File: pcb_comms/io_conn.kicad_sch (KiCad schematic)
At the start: 15 parts, among them IC1 CP2102N-A02-GQFN28, J1 Conn_01x06_Pin, J2 USB_B_Micro

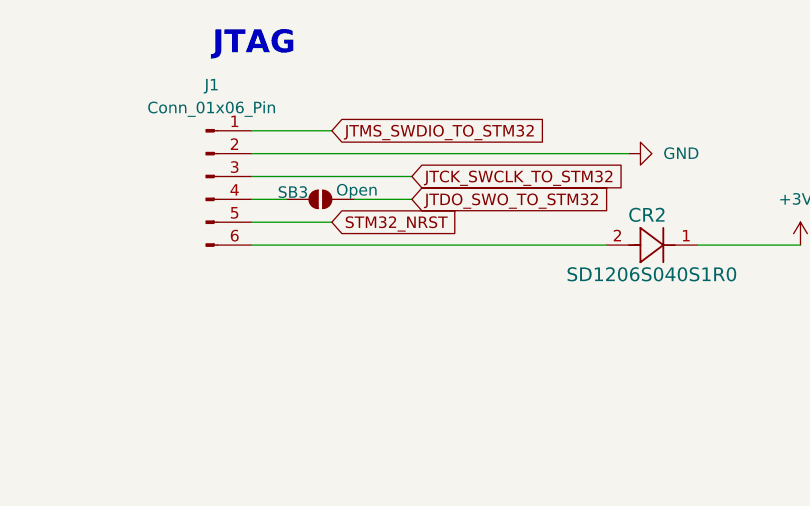
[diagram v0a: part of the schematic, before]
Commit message: Add external circuit for gps
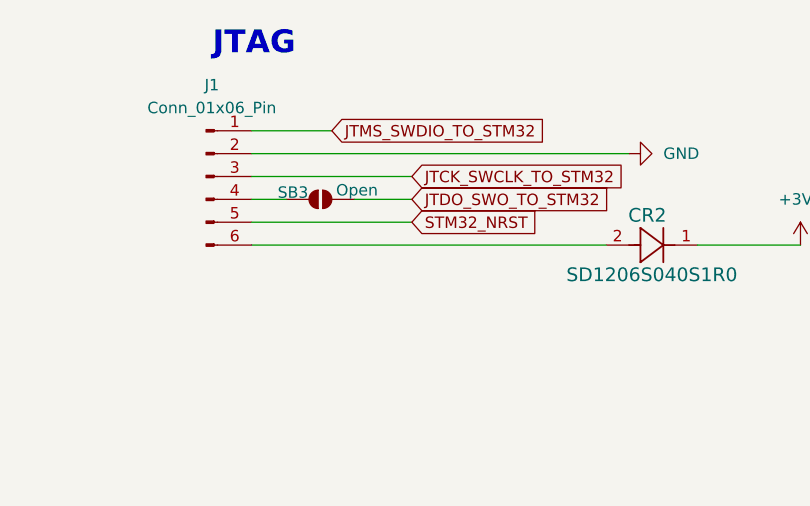
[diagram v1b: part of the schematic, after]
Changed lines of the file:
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@@
 	(wire
 		(pts
-			(xy 208.28 39.37) (xy 217.17 39.37)
+			(xy 208.28 39.37) (xy 226.06 39.37)
 		)
 		(stroke
@@
 	(global_label "STM32_NRST"
 		(shape input)
-		(at 217.17 39.37 0)
+		(at 226.06 39.37 0)
 		(fields_autoplaced yes)
 		(effects
@@
 		)
 		(property "Intersheetrefs" "${INTERSHEET_REFS}"
-			(at 231.9479 39.37 0)
+			(at 240.8379 39.37 0)
 			(effects
 				(font

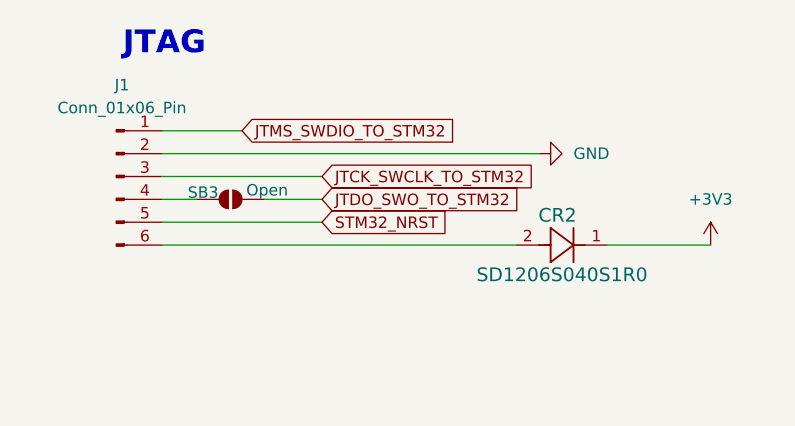
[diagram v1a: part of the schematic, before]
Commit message: Update GPS to pasive antenna
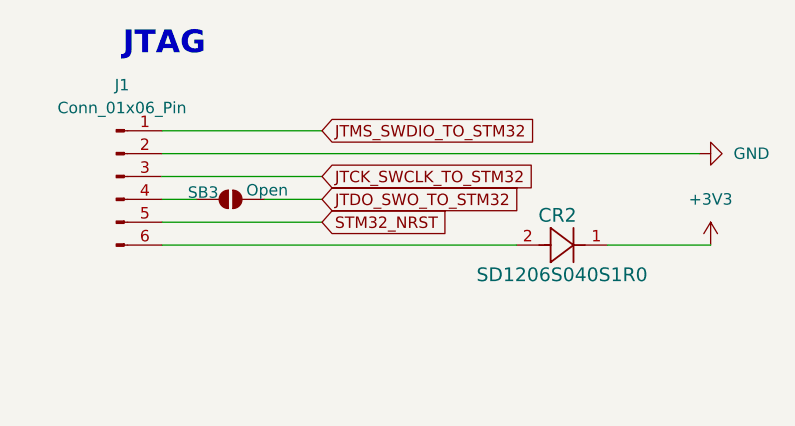
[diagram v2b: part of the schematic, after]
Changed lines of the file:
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@@
 	(wire
 		(pts
-			(xy 208.28 29.21) (xy 217.17 29.21)
+			(xy 208.28 29.21) (xy 226.06 29.21)
 		)
 		(stroke
@@
 	(wire
 		(pts
-			(xy 208.28 31.75) (xy 250.19 31.75)
+			(xy 208.28 31.75) (xy 267.97 31.75)
 		)
 		(stroke
@@
 	(global_label "JTMS_SWDIO_TO_STM32"
 		(shape input)
-		(at 217.17 29.21 0)
+		(at 226.06 29.21 0)
 		(fields_autoplaced yes)
 		(effects
@@
 		)
 		(property "Intersheetrefs" "${INTERSHEET_REFS}"
-			(at 241.8659 29.21 0)
+			(at 250.7559 29.21 0)
 			(effects
 				(font
@@
 	(symbol
 		(lib_id "power:GND")
-		(at 250.19 31.75 90)
+		(at 267.97 31.75 90)
 		(unit 1)
 		(exclude_from_sim no)
@@
 		(fields_autoplaced yes)
 		(property "Reference" "#PWR042"
-			(at 256.54 31.75 0)
+			(at 274.32 31.75 0)
 			(effects
 				(font
@@
 		)
 		(property "Value" "GND"
-			(at 254 31.7499 90)
+			(at 271.78 31.7499 90)
 			(effects
 				(font
@@
 		)
 		(property "Footprint" ""
-			(at 250.19 31.75 0)
+			(at 267.97 31.75 0)
 			(effects
 				(font
@@
 		)
 		(property "Datasheet" ""
-			(at 250.19 31.75 0)
+			(at 267.97 31.75 0)
 			(effects
 				(font
@@
 		)
 		(property "Description" "Power symbol creates a global label with name \"GND\" , ground"
-			(at 250.19 31.75 0)
-			(effects
-				(font
+			(at 267.97 31.75 0)
+			(effects
+				(font

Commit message: Update GPS
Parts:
- added J3, J5: OBC_I2C, symbol Connector_Generic:Conn_01x02
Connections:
- net GND: now also J5.2 (Pin_2)
- new net I2C1_SCL: J3.1 (Pin_1)
- new net I2C1_SDA: J3.2 (Pin_2)
- new net VBAT: J5.1 (Pin_1)
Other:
- note added: "FROM EPS"
- note added: "TO OBC"

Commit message: Add antenna deploy
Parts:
- added C47: 100uF, symbol Device:C
- added C48: 10uF, symbol Device:C
- added D6: Green, symbol Device:LED
- added J6: OBC_I2C, symbol Connector_Generic:Conn_01x02
- added R9: 1k, Resistor_SMD:R_0805_2012Metric, symbol Device:R
- added U6: ADP122AUJZ-3.3-R7, ADP122AUJZ_3_3_R7:UJ_5_ADI, symbol LDO_ADP122AUJZ_3_3_R7:ADP122AUJZ-3.3-R7
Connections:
- net GND: now also C47.2, C48.2, J6.2 (Pin_2), R9.1, U6.2 (GND)
- net USB_5V: now also C47.1, U6.1 (VIN), U6.3 (EN)
- net +3.3V renamed +3.3V_USB
- net +3.3V_USB: now also C48.1, D6.2 (A), U6.5 (VOUT)
- new net: D6.1 (K), R9.2
- new net BATT_FULL: J6.1 (Pin_1)
- no-connect marks 18 -> 19
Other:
- note added: "LDO 5V TO 3V3 (USB)"

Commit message: Update USB
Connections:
- net VBUS: now reaches CR1.2, D2.2 (K), J2.1 (VBUS)
- net VBUS: now also R2.1
- net +3.3V_USB renamed +3.3V
- net USB_5V renamed +5V
- net +5V: no longer R2.1

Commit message: Last update
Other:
- company: (none) -> Sanie Peralta, Alejandro Campo
- title: (none) -> PC1: APRS & GPS
- moved on the sheet: C48, D6, R9
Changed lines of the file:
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@@
 	(generator_version "9.0")
 	(paper "A4")
+	(title_block
+		(title "PC1: APRS & GPS")
+		(date "2026-04-01")
+		(rev "1.0")
+		(company "Sanie Peralta, Alejandro Campo")
+		(comment 1 "Introducción a la Ingeniería Satelital ")
+		(comment 2 "Primer Parcial")
+	)
 	(text "TO OBC"
 		(exclude_from_sim no)
@@
 	)
 	(junction
-		(at 135.89 161.29)
+		(at 124.46 161.29)
 		(diameter 0)
 		(color 0 0 0 0)
@@
 	)
 	(junction
-		(at 120.65 161.29)
+		(at 109.22 161.29)
 		(diameter 0)
 		(color 0 0 0 0)
@@
 	(wire
 		(pts
-			(xy 135.89 161.29) (xy 148.59 161.29)
+			(xy 124.46 161.29) (xy 137.16 161.29)
 		)
 		(stroke
@@
 	(wire
 		(pts
-			(xy 120.65 161.29) (xy 135.89 161.29)
+			(xy 109.22 161.29) (xy 124.46 161.29)
 		)
 		(stroke
@@
 	(wire
 		(pts
-			(xy 120.65 170.18) (xy 120.65 177.8)
+			(xy 109.22 170.18) (xy 109.22 177.8)
 		)
 		(stroke
@@
 	(wire
 		(pts
-			(xy 135.89 163.83) (xy 135.89 161.29)
+			(xy 124.46 163.83) (xy 124.46 161.29)
 		)
 		(stroke
@@
 	(wire
 		(pts
-			(xy 120.65 162.56) (xy 120.65 161.29)
+			(xy 109.22 162.56) (xy 109.22 161.29)
 		)
 		(stroke
@@
 	(wire
 		(pts
-			(xy 102.87 161.29) (xy 120.65 161.29)
+			(xy 102.87 161.29) (xy 109.22 161.29)
 		)
 		(stroke
@@
 	(wire
 		(pts
-			(xy 135.89 171.45) (xy 135.89 173.99)
+			(xy 124.46 171.45) (xy 124.46 173.99)
 		)
 		(stroke
@@
 	(wire
 		(pts
-			(xy 120.65 185.42) (xy 120.65 187.96)
+			(xy 109.22 185.42) (xy 109.22 187.96)
 		)
 		(stroke
@@
 	(symbol
 		(lib_id "Device:R")
-		(at 120.65 181.61 180)
+		(at 109.22 181.61 180)
 		(unit 1)
 		(exclude_from_sim no)
@@
 		(fields_autoplaced yes)
 		(property "Reference" "R9"
-			(at 123.19 180.3399 0)
+			(at 111.76 180.3399 0)
 			(effects
 				(font
@@
 		)
 		(property "Value" "1k"
-			(at 123.19 182.8799 0)
+			(at 111.76 182.8799 0)
 			(effects
 				(font
@@
 		)
 		(property "Footprint" "Resistor_SMD:R_0805_2012Metric"
-			(at 122.428 181.61 90)
+			(at 110.998 181.61 90)
 			(effects
 				(font
@@
 		)
 		(property "Datasheet" "~"
-			(at 120.65 181.61 0)
+			(at 109.22 181.61 0)
 			(effects
 				(font
@@
 		)
 		(property "Description" "Resistor"
-			(at 120.65 181.61 0)
+			(at 109.22 181.61 0)
 			(effects
 				(font
@@
 		)
 		(property "AVAILABILITY" ""
-			(at 120.65 181.61 0)
+			(at 109.22 181.61 0)
 			(effects
 				(font
@@
 		)
 		(property "DESCRIPTION" ""
-			(at 120.65 181.61 0)
+			(at 109.22 181.61 0)
 			(effects
 				(font
@@
 		)
 		(property "PACKAGE" ""
-			(at 120.65 181.61 0)
+			(at 109.22 181.61 0)
 			(effects
 				(font
@@
 		)
 		(property "PART_REV" ""
-			(at 120.65 181.61 0)
+			(at 109.22 181.61 0)
 			(effects
 				(font
@@
 		)
 		(property "PRICE" ""
-			(at 120.65 181.61 0)
+			(at 109.22 181.61 0)
 			(effects
 				(font
@@
 	(symbol
 		(lib_id "power:+3.3V")
-		(at 148.59 161.29 270)
+		(at 137.16 161.29 270)
 		(unit 1)
 		(exclude_from_sim no)
@@
 		(dnp no)
 		(property "Reference" "#PWR044"
-			(at 144.78 161.29 0)
+			(at 133.35 161.29 0)
 			(effects
 				(font
@@
 		)
 		(property "Value" "+3.3V"
-			(at 154.686 161.036 90)
+			(at 143.256 161.036 90)
 			(effects
 				(font
@@
 		)
 		(property "Footprint" ""
-			(at 148.59 161.29 0)
+			(at 137.16 161.29 0)
 			(effects
 				(font
@@
 		)
 		(property "Datasheet" ""
-			(at 148.59 161.29 0)
+			(at 137.16 161.29 0)
 			(effects
 				(font
@@
 		)
 		(property "Description" "Power symbol creates a global label with name \"+3.3V\""
-			(at 148.59 161.29 0)
+			(at 137.16 161.29 0)
 			(effects
 				(font
@@
 	(symbol
 		(lib_id "Device:C")
-		(at 135.89 167.64 0)
+		(at 124.46 167.64 0)
 		(unit 1)
 		(exclude_from_sim no)
@@
 		(dnp no)
 		(property "Reference" "C48"
-			(at 138.43 166.878 0)
+			(at 127 166.878 0)
 			(effects
 				(font
@@
 		)
 		(property "Value" "10uF"
-			(at 138.43 169.418 0)
+			(at 127 169.418 0)
 			(effects
 				(font
@@
 		)
 		(property "Footprint" ""
-			(at 136.8552 171.45 0)
+			(at 125.4252 171.45 0)
 			(effects
 				(font
@@
 		)
 		(property "Datasheet" "~"
-			(at 135.89 167.64 0)
+			(at 124.46 167.64 0)
 			(effects
 				(font
@@
 		)
 		(property "Description" "Unpolarized capacitor"
-			(at 135.89 167.64 0)
+			(at 124.46 167.64 0)
 			(effects
 				(font
@@
 	(symbol
 		(lib_id "power:GND")
-		(at 120.65 187.96 0)
+		(at 109.22 187.96 0)
 		(unit 1)
 		(exclude_from_sim no)
@@
 		(fields_autoplaced yes)
 		(property "Reference" "#PWR058"
-			(at 120.65 194.31 0)
+			(at 109.22 194.31 0)
 			(effects
 				(font
@@
 		)
 		(property "Value" "GND"
-			(at 120.65 193.04 0)
+			(at 109.22 193.04 0)
 			(effects
 				(font
@@
 		)
 		(property "Footprint" ""
-			(at 120.65 187.96 0)
+			(at 109.22 187.96 0)
 			(effects
 				(font
@@
 		)
 		(property "Datasheet" ""
-			(at 120.65 187.96 0)
+			(at 109.22 187.96 0)
 			(effects
 				(font
@@
 		)
 		(property "Description" "Power symbol creates a global label with name \"GND\" , ground"
-			(at 120.65 187.96 0)
+			(at 109.22 187.96 0)
 			(effects
 				(font
@@
 	(symbol
 		(lib_id "power:GND")
-		(at 135.89 173.99 0)
+		(at 124.46 173.99 0)
 		(unit 1)
 		(exclude_from_sim no)
@@
 		(fields_autoplaced yes)
 		(property "Reference" "#PWR059"
-			(at 135.89 180.34 0)
+			(at 124.46 180.34 0)
 			(effects
 				(font
@@
 		)
 		(property "Value" "GND"
-			(at 135.89 179.07 0)
+			(at 124.46 179.07 0)
 			(effects
 				(font
@@
 		)
 		(property "Footprint" ""
-			(at 135.89 173.99 0)
+			(at 124.46 173.99 0)
 			(effects
 				(font
@@
 		)
 		(property "Datasheet" ""
-			(at 135.89 173.99 0)
+			(at 124.46 173.99 0)
 			(effects
 				(font
@@
 		)
 		(property "Description" "Power symbol creates a global label with name \"GND\" , ground"
-			(at 135.89 173.99 0)
+			(at 124.46 173.99 0)
 			(effects
 				(font
@@
 	(symbol
 		(lib_id "Device:LED")
-		(at 120.65 166.37 270)
+		(at 109.22 166.37 270)
 		(mirror x)
 		(unit 1)
@@
 		(fields_autoplaced yes)
 		(property "Reference" "D6"
-			(at 123.19 166.6874 90)
+			(at 111.76 166.6874 90)
 			(effects
 				(font
@@
 		)
 		(property "Value" "Green"
-			(at 123.19 169.2274 90)
+			(at 111.76 169.2274 90)
 			(effects
 				(font
@@
 		)
 		(property "Footprint" ""
-			(at 120.65 166.37 0)
+			(at 109.22 166.37 0)
 			(effects
 				(font
@@
 		)
 		(property "Datasheet" "~"
-			(at 120.65 166.37 0)
+			(at 109.22 166.37 0)
 			(effects
 				(font
@@
 		)
 		(property "Description" "Light emitting diode"
-			(at 120.65 166.37 0)
+			(at 109.22 166.37 0)
 			(effects
 				(font
@@
 		)
 		(property "Sim.Pins" "1=K 2=A"
-			(at 120.65 166.37 0)
+			(at 109.22 166.37 0)
 			(effects
 				(font

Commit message: rev 1.1
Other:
- moved on the sheet: J3, J5, J6
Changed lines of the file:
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@@
 	(text "TO OBC"
 		(exclude_from_sim no)
-		(at 212.344 63.5 0)
+		(at 235.204 68.58 0)
 		(effects
 			(font
@@
 	(text "FROM EPS"
 		(exclude_from_sim no)
-		(at 212.09 87.376 0)
+		(at 234.95 92.456 0)
 		(effects
 			(font
@@
 	(wire
 		(pts
-			(xy 191.77 92.71) (xy 208.28 92.71)
+			(xy 214.63 97.79) (xy 231.14 97.79)
 		)
 		(stroke
@@
 	(wire
 		(pts
-			(xy 193.04 111.76) (xy 208.28 111.76)
+			(xy 215.9 116.84) (xy 231.14 116.84)
 		)
 		(stroke
@@
 	(wire
 		(pts
-			(xy 191.77 95.25) (xy 208.28 95.25)
+			(xy 214.63 100.33) (xy 231.14 100.33)
 		)
 		(stroke
@@
 	(wire
 		(pts
-			(xy 191.77 71.12) (xy 208.28 71.12)
+			(xy 214.63 76.2) (xy 231.14 76.2)
 		)
 		(stroke
@@
 	(wire
 		(pts
-			(xy 193.04 114.3) (xy 208.28 114.3)
+			(xy 215.9 119.38) (xy 231.14 119.38)
 		)
 		(stroke
@@
 	(wire
 		(pts
-			(xy 191.77 73.66) (xy 208.28 73.66)
+			(xy 214.63 78.74) (xy 231.14 78.74)
 		)
 		(stroke
@@
 	(global_label "VBAT"
 		(shape input)
-		(at 191.77 92.71 180)
+		(at 214.63 97.79 180)
 		(fields_autoplaced yes)
 		(effects
@@
 		)
 		(property "Intersheetrefs" "${INTERSHEET_REFS}"
-			(at 184.37 92.71 0)
+			(at 207.23 97.79 0)
 			(effects
 				(font
@@
 	(global_label "I2C1_SDA"
 		(shape input)
-		(at 191.77 73.66 180)
+		(at 214.63 78.74 180)
 		(fields_autoplaced yes)
 		(effects
@@
 		)
 		(property "Intersheetrefs" "${INTERSHEET_REFS}"
-			(at 179.9553 73.66 0)
+			(at 202.8153 78.74 0)
 			(effects
 				(font
@@
 	(global_label "I2C1_SCL"
 		(shape input)
-		(at 191.77 71.12 180)
+		(at 214.63 76.2 180)
 		(fields_autoplaced yes)
 		(effects
@@
 		)
 		(property "Intersheetrefs" "${INTERSHEET_REFS}"
-			(at 180.0158 71.12 0)
+			(at 202.8758 76.2 0)
 			(effects
 				(font
@@
 	(global_label "BATT_FULL"
 		(shape input)
-		(at 193.04 111.76 180)
+		(at 215.9 116.84 180)
 		(fields_autoplaced yes)
 		(effects
@@
 		)
 		(property "Intersheetrefs" "${INTERSHEET_REFS}"
-			(at 180.3181 111.76 0)
+			(at 203.1781 116.84 0)
 			(effects
 				(font
@@
 	(symbol
 		(lib_id "Connector_Generic:Conn_01x02")
-		(at 213.36 71.12 0)
+		(at 236.22 76.2 0)
 		(unit 1)
 		(exclude_from_sim no)
@@
 		(fields_autoplaced yes)
 		(property "Reference" "J3"
-			(at 215.9 71.1199 0)
+			(at 238.76 76.1999 0)
 			(effects
 				(font
@@
 		)
 		(property "Value" "OBC_I2C"
-			(at 215.9 73.6599 0)
+			(at 238.76 78.7399 0)
 			(effects
 				(font
@@
 		)
 		(property "Footprint" ""
-			(at 213.36 71.12 0)
+			(at 236.22 76.2 0)
 			(effects
 				(font
@@
 		)
 		(property "Datasheet" "~"
-			(at 213.36 71.12 0)
+			(at 236.22 76.2 0)
 			(effects
 				(font
@@
 		)
 		(property "Description" "Generic connector, single row, 01x02, script generated (kicad-library-utils/schlib/autogen/connector/)"
-			(at 213.36 71.12 0)
+			(at 236.22 76.2 0)
 			(effects
 				(font
@@
 	(symbol
 		(lib_id "Connector_Generic:Conn_01x02")
-		(at 213.36 92.71 0)
+		(at 236.22 97.79 0)
 		(unit 1)
 		(exclude_from_sim no)
@@
 		(fields_autoplaced yes)
 		(property "Reference" "J5"
-			(at 215.9 92.7099 0)
+			(at 238.76 97.7899 0)
 			(effects
 				(font
@@
 		)
 		(property "Value" "OBC_I2C"
-			(at 215.9 95.2499 0)
+			(at 238.76 100.3299 0)
 			(effects
 				(font
@@
 		)
 		(property "Footprint" ""
-			(at 213.36 92.71 0)
+			(at 236.22 97.79 0)
 			(effects
 				(font
@@
 		)
 		(property "Datasheet" "~"
-			(at 213.36 92.71 0)
+			(at 236.22 97.79 0)
 			(effects
 				(font
@@
 		)
 		(property "Description" "Generic connector, single row, 01x02, script generated (kicad-library-utils/schlib/autogen/connector/)"
-			(at 213.36 92.71 0)
+			(at 236.22 97.79 0)
 			(effects
 				(font
@@
 	(symbol
 		(lib_id "power:GND")
-		(at 193.04 114.3 270)
+		(at 215.9 119.38 270)
 		(unit 1)
 		(exclude_from_sim no)
@@
 		(fields_autoplaced yes)
 		(property "Reference" "#PWR069"
-			(at 186.69 114.3 0)
+			(at 209.55 119.38 0)
 			(effects
 				(font
@@
 		)
 		(property "Value" "GND"
-			(at 189.23 114.2999 90)
+			(at 212.09 119.3799 90)
 			(effects
 				(font
@@
 		)
 		(property "Footprint" ""
-			(at 193.04 114.3 0)
+			(at 215.9 119.38 0)
 			(effects
 				(font
@@
 		)
 		(property "Datasheet" ""
-			(at 193.04 114.3 0)
+			(at 215.9 119.38 0)
 			(effects
 				(font
@@
 		)
 		(property "Description" "Power symbol creates a global label with name \"GND\" , ground"
-			(at 193.04 114.3 0)
+			(at 215.9 119.38 0)
 			(effects
 				(font
@@
 	(symbol
 		(lib_id "Connector_Generic:Conn_01x02")
-		(at 213.36 111.76 0)
+		(at 236.22 116.84 0)
 		(unit 1)
 		(exclude_from_sim no)
@@
 		(fields_autoplaced yes)
 		(property "Reference" "J6"
-			(at 215.9 111.7599 0)
+			(at 238.76 116.8399 0)
 			(effects
 				(font
@@
 		)
 		(property "Value" "OBC_I2C"
-			(at 215.9 114.2999 0)
+			(at 238.76 119.3799 0)
 			(effects
 				(font
@@
 		)
 		(property "Footprint" ""
-			(at 213.36 111.76 0)
+			(at 236.22 116.84 0)
 			(effects
 				(font
@@
 		)
 		(property "Datasheet" "~"
-			(at 213.36 111.76 0)
+			(at 236.22 116.84 0)
 			(effects
 				(font
@@
 		)
 		(property "Description" "Generic connector, single row, 01x02, script generated (kicad-library-utils/schlib/autogen/connector/)"
-			(at 213.36 111.76 0)
+			(at 236.22 116.84 0)
 			(effects
 				(font
@@
 	(symbol
 		(lib_id "power:GND")
-		(at 191.77 95.25 270)
+		(at 214.63 100.33 270)
 		(unit 1)
 		(exclude_from_sim no)
@@
 		(fields_autoplaced yes)
 		(property "Reference" "#PWR051"
-			(at 185.42 95.25 0)
+			(at 208.28 100.33 0)
 			(effects
 				(font
@@
 		)
 		(property "Value" "GND"
-			(at 187.96 95.2499 90)
+			(at 210.82 100.3299 90)
 			(effects
 				(font
@@
 		)
 		(property "Footprint" ""
-			(at 191.77 95.25 0)
+			(at 214.63 100.33 0)
 			(effects
 				(font
@@
 		)
 		(property "Datasheet" ""
-			(at 191.77 95.25 0)
+			(at 214.63 100.33 0)
 			(effects
 				(font
@@
 		)
 		(property "Description" "Power symbol creates a global label with name \"GND\" , ground"
-			(at 191.77 95.25 0)
+			(at 214.63 100.33 0)
 			(effects
 				(font
